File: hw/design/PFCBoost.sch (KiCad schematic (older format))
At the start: 34 parts

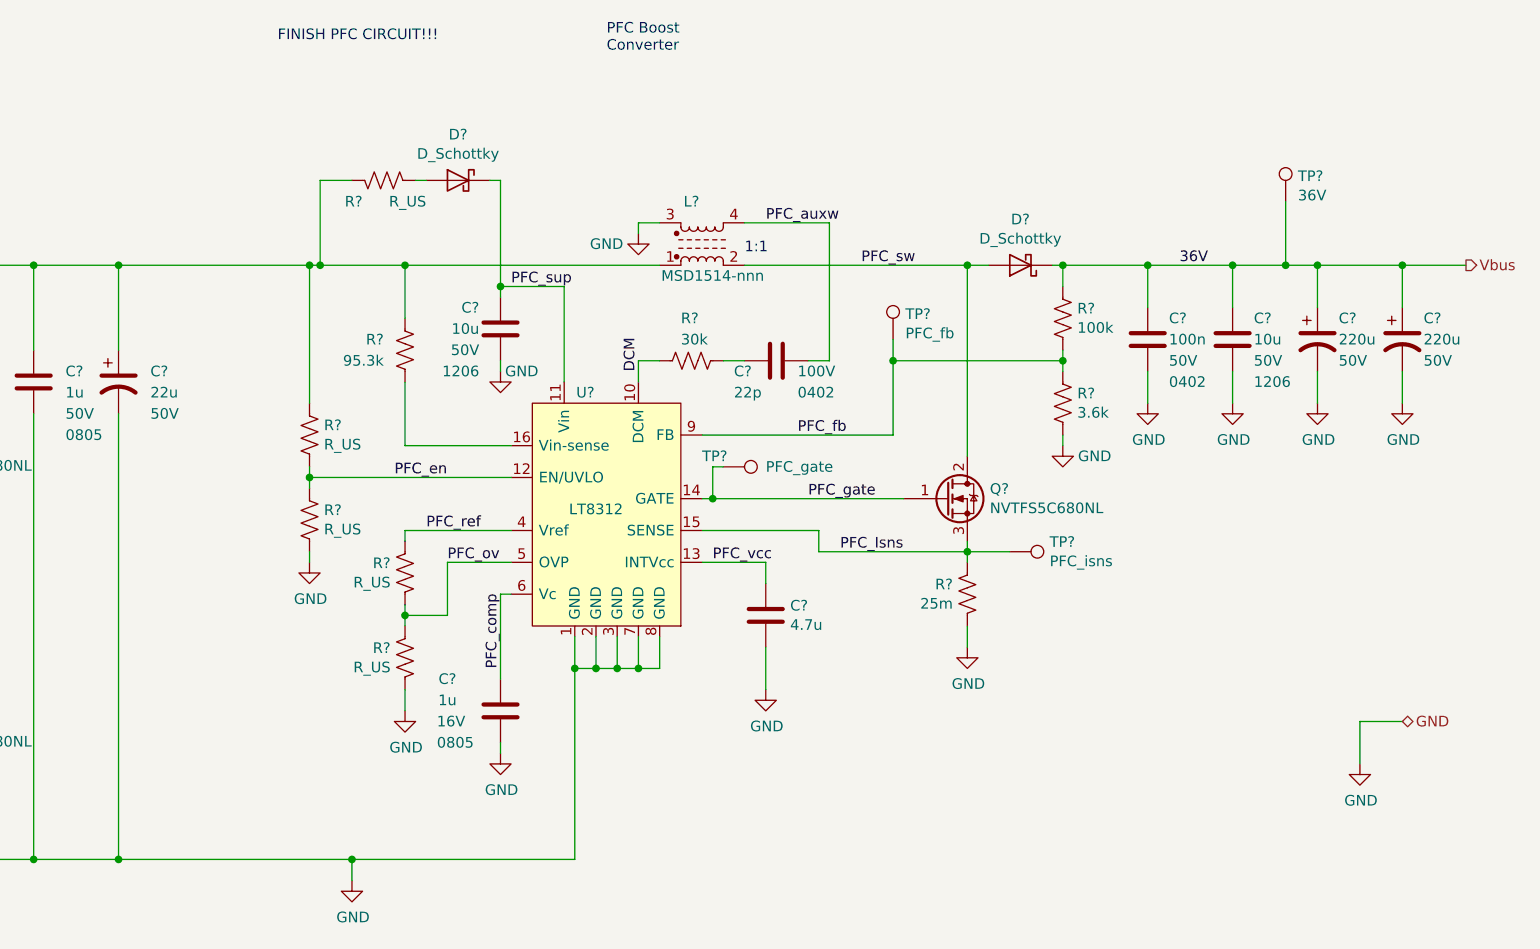
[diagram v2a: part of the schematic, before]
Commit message: lots of work
expanded README doc, specifications, added secondary regulator circuit + symbol, more component specs added
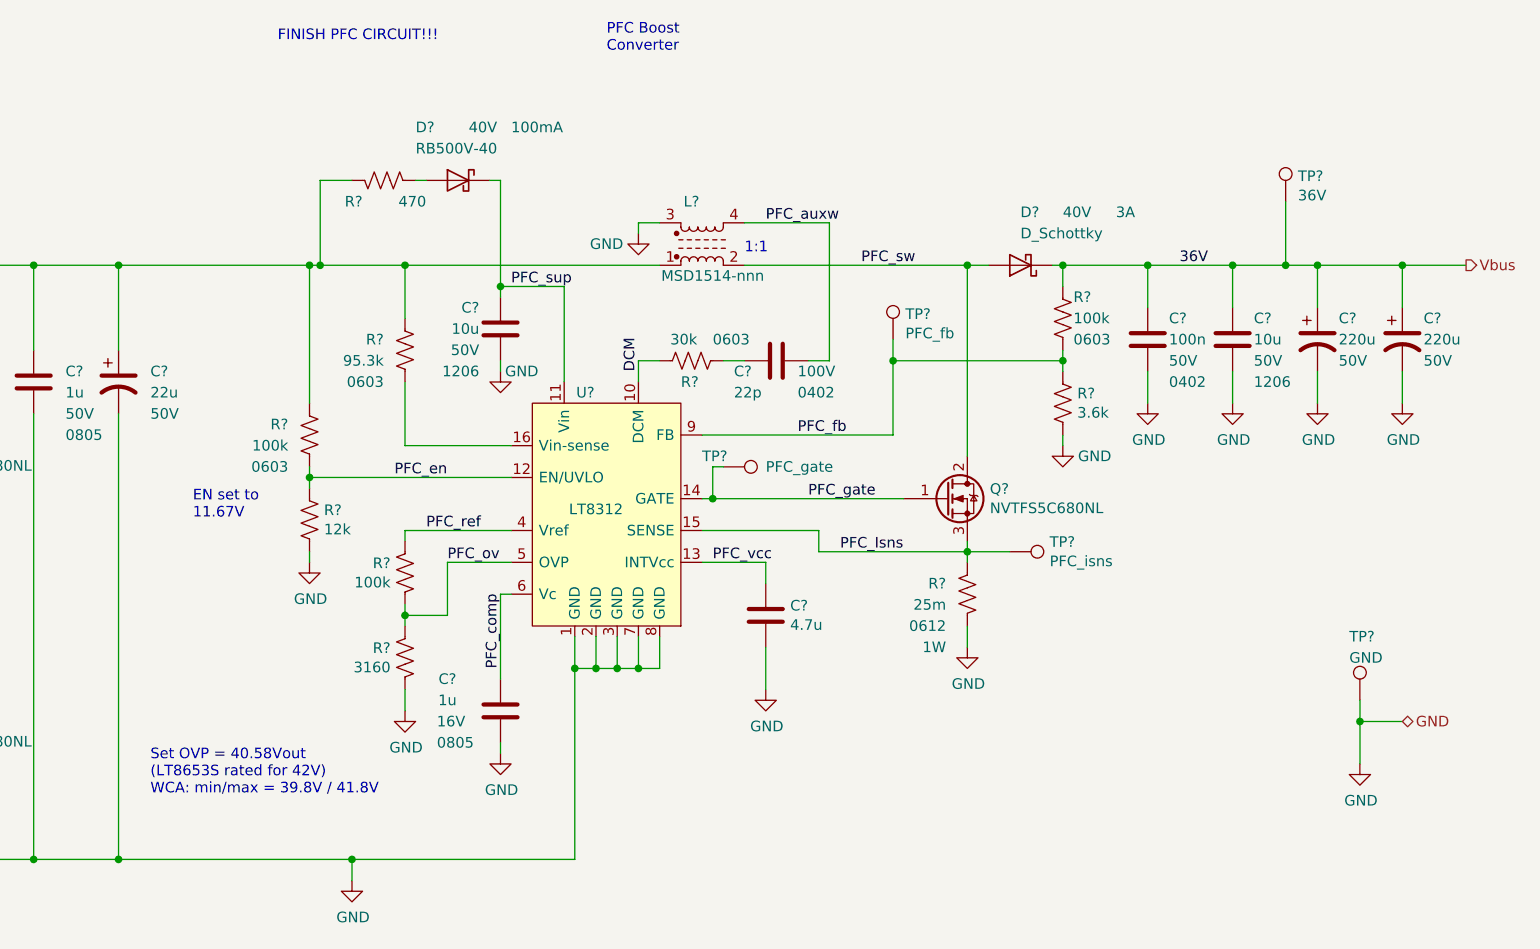
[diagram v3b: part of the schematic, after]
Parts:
- removed R?: R_US, Resistor_SMD:R_0603_1608Metric, symbol Device:R_US
- added R?: 100k, Resistor_SMD:R_0805_2012Metric_Pad1.15x1.40mm_HandSolder, symbol Device:R_US
- added TP?: GND, TestPoint:TestPoint_Keystone_5000-5004_Miniature, symbol Connector:TestPoint
- D?: value D_Schottky -> RB500V-40; MfrNum (none) -> TSMC_RB500V-40
- R?: value R_US -> 3160
- R?: value R_US -> 100k
- R?: PRating (none) -> 1W; Size (none) -> 0612
- R?: footprint Resistor_SMD:R_0805_2012Metric_Pad1.15x1.40mm_HandSolder -> Resistor_SMD:R_0805_2012Metric; Size (none) -> 0603
- R?: value R_US -> 12k
- R?: footprint Resistor_SMD:R_0603_1608Metric -> Resistor_SMD:R_0805_2012Metric; Size (none) -> 0603
- R?: value R_US -> 470; footprint Resistor_SMD:R_0603_1608Metric -> Resistor_SMD:R_0805_2012Metric
- R?: Size (none) -> 0603; VRating (none) -> 50
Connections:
- net GND: now also TP?.1
- net PFC_en: now also R?.2
- net P_rect: now also R?.1
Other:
- note added: "EN set to\n11.67V"
- note added: "Set OVP = 40.58Vout\n(LT8653S rated for 42V)\nWCA: min/max = 39.8V / 41.8V"
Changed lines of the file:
@@
 P 5900 3800
 F 0 "R?" H 5832 3754 50  0000 R CNN
-F 1 "R_US" H 5832 3845 50  0000 R CNN
+F 1 "3160" H 5832 3845 50  0000 R CNN
 F 2 "Resistor_SMD:R_0603_1608Metric" V 5940 3790 50  0001 C CNN
 F 3 "~" H 5900 3800 50  0001 C CNN
@@
 P 5900 3400
 F 0 "R?" H 5832 3354 50  0000 R CNN
-F 1 "R_US" H 5832 3445 50  0000 R CNN
+F 1 "100k" H 5832 3445 50  0000 R CNN
 F 2 "Resistor_SMD:R_0603_1608Metric" V 5940 3390 50  0001 C CNN
 F 3 "~" H 5900 3400 50  0001 C CNN
@@
 Connection ~ 4150 4750
 Wire Wire Line
-	4150 4750 4550 4750
-Wire Wire Line
 	4550 2650 4550 4750
-Connection ~ 4550 4750
 Wire Wire Line
 	6350 4200 6350 4250
@@
 U 1 1 5E8396C6
 P 8550 3500
-F 0 "R?" H 8482 3454 50  0000 R CNN
-F 1 "25m" H 8482 3545 50  0000 R CNN
+F 0 "R?" H 8450 3450 50  0000 R CNN
+F 1 "25m" H 8450 3550 50  0000 R CNN
 F 2 "Resistor_SMD:R_0612_1632Metric" V 8590 3490 50  0001 C CNN
 F 3 "~" H 8550 3500 50  0001 C CNN
+F 4 "0612" H 8450 3650 50  0000 R CNN "Size"
+F 5 "1W" H 8450 3750 50  0000 R CNN "PRating"
 	1    8550 3500
 	1    0    0    1
@@
 U 1 1 5EB6C5FB
 P 9000 2200
-F 0 "R?" H 8932 2154 50  0000 R CNN
-F 1 "100k" H 8932 2245 50  0000 R CNN
-F 2 "Resistor_SMD:R_0805_2012Metric_Pad1.15x1.40mm_HandSolder" V 9040 2190 50  0001 C CNN
+F 0 "R?" H 8950 2100 50  0000 R CNN
+F 1 "100k" H 8950 2200 50  0000 R CNN
+F 2 "Resistor_SMD:R_0805_2012Metric" V 9040 2190 50  0001 C CNN
 F 3 "~" H 9000 2200 50  0001 C CNN
+F 4 "0603" H 8950 2300 50  0000 R CNN "Size"
 	1    9000 2200
 	-1   0    0    1
@@
 $Comp
 L Device:R_US R?
-U 1 1 5EB79CFA
-P 5450 2750
-F 0 "R?" H 5382 2704 50  0000 R CNN
-F 1 "R_US" H 5382 2795 50  0000 R CNN
-F 2 "Resistor_SMD:R_0603_1608Metric" V 5490 2740 50  0001 C CNN
-F 3 "~" H 5450 2750 50  0001 C CNN
-	1    5450 2750
-	-1   0    0    1
-$EndComp
-$Comp
-L Device:R_US R?
 U 1 1 5EB79D44
 P 5450 3150
 F 0 "R?" H 5382 3104 50  0000 R CNN
-F 1 "R_US" H 5382 3195 50  0000 R CNN
+F 1 "12k" H 5382 3195 50  0000 R CNN
 F 2 "Resistor_SMD:R_0603_1608Metric" V 5490 3140 50  0001 C CNN
 F 3 "~" H 5450 3150 50  0001 C CNN
@@
 $EndComp
 $Comp
-L Device:R_US R?
-U 1 1 5EBD6503
-P 7250 2400
-F 0 "R?" V 7450 2450 50  0000 R CNN
-F 1 "30k" V 7350 2450 50  0000 R CNN
-F 2 "Resistor_SMD:R_0603_1608Metric" V 7290 2390 50  0001 C CNN
-F 3 "~" H 7250 2400 50  0001 C CNN
-	1    7250 2400
-	0    -1   -1   0
-$EndComp
-$Comp
 L power:GND #PWR?
 U 1 1 5EC0311F
@@
 Wire Wire Line
 	4550 1950 5450 1950
-Wire Wire Line
-	4550 4750 5650 4750
 $Comp
 L Device:R_US R?
@@
 P 5800 1550
 F 0 "R?" V 5700 1450 50  0000 R CNN
-F 1 "R_US" V 5700 1750 50  0000 R CNN
-F 2 "Resistor_SMD:R_0603_1608Metric" V 5840 1540 50  0001 C CNN
+F 1 "470" V 5700 1750 50  0000 R CNN
+F 2 "Resistor_SMD:R_0805_2012Metric" V 5840 1540 50  0001 C CNN
 F 3 "~" H 5800 1550 50  0001 C CNN
 	1    5800 1550
@@
 U 1 1 5EBAA43A
 P 8800 1950
-F 0 "D?" H 8800 1734 50  0000 C CNN
-F 1 "D_Schottky" H 8800 1825 50  0000 C CNN
+F 0 "D?" H 8800 1700 50  0000 R CNN
+F 1 "D_Schottky" H 8800 1800 50  0000 R CNN
 F 2 "Diode_SMD:D_SMB" H 8800 1950 50  0001 C CNN
 F 3 "~" H 8800 1950 50  0001 C CNN
-F 4 "40V" H 8800 1950 50  0001 C CNN "VRating"
-F 5 "3A" H 8800 1950 50  0001 C CNN "IRating"
+F 4 "40V" H 8600 1700 50  0000 R CNN "VRating"
+F 5 "3A" H 8350 1700 50  0000 R CNN "IRating"
 	1    8800 1950
 	-1   0    0    1
@@
 U 1 1 5EBF8B82
 P 6150 1550
-F 0 "D?" H 6150 1766 50  0000 C CNN
-F 1 "D_Schottky" H 6150 1675 50  0000 C CNN
+F 0 "D?" H 6350 1800 50  0000 R CNN
+F 1 "RB500V-40" H 6350 1700 50  0000 R CNN
 F 2 "Diode_SMD:D_SOD-123" H 6150 1550 50  0001 C CNN
 F 3 "~" H 6150 1550 50  0001 C CNN
-F 4 "40V" H 6150 1550 50  0001 C CNN "VRating"
-F 5 "100mA" H 6150 1550 50  0001 C CNN "IRating"
+F 4 "40V" H 6100 1800 50  0000 R CNN "VRating"
+F 5 "100mA" H 5900 1800 50  0000 R CNN "IRating"
+F 6 "TSMC_RB500V-40" H 6150 1550 50  0001 C CNN "MfrNum"
 	1    6150 1550
 	-1   0    0    -1
@@
 F 2 "Resistor_SMD:R_0805_2012Metric_Pad1.15x1.40mm_HandSolder" V 5940 2340 50  0001 C CNN
 F 3 "~" H 5900 2350 50  0001 C CNN
+F 4 "50" H 5900 2350 50  0001 C CNN "VRating"
+F 5 "0603" H 5800 2200 50  0000 R CNN "Size"
 	1    5900 2350
 	1    0    0    -1
@@
 Wire Wire Line
 	7500 1750 7900 1750
+$Comp
+L Device:R_US R?
+U 1 1 5EC990DA
+P 5450 2750
+F 0 "R?" H 5350 2800 50  0000 R CNN
+F 1 "100k" H 5350 2700 50  0000 R CNN
+F 2 "Resistor_SMD:R_0805_2012Metric_Pad1.15x1.40mm_HandSolder" V 5490 2740 50  0001 C CNN
+F 3 "~" H 5450 2750 50  0001 C CNN
+F 4 "50" H 5450 2750 50  0001 C CNN "VRating"
+F 5 "0603" H 5350 2600 50  0000 R CNN "Size"
+	1    5450 2750
+	1    0    0    -1
+$EndComp
+Connection ~ 4550 4750
+Wire Wire Line
+	4550 4750 5650 4750
+Wire Wire Line
+	4150 4750 4550 4750
+$Comp
+L Device:R_US R?
+U 1 1 5EBD6503
+P 7250 2400
+F 0 "R?" V 7150 2450 50  0000 R CNN
+F 1 "30k" V 7350 2500 50  0000 R CNN
+F 2 "Resistor_SMD:R_0805_2012Metric" V 7290 2390 50  0001 C CNN
+F 3 "~" H 7250 2400 50  0001 C CNN
+F 4 "0603" V 7350 2300 50  0000 R CNN "Size"
+	1    7250 2400
+	0    -1   -1   0
+$EndComp
+$Comp
+L Connector:TestPoint TP?
+U 1 1 5ECC8F09
+P 10400 4000
+AR Path="/5E80D1C0/5ECC8F09" Ref="TP?"  Part="1"
+AR Path="/5E80D210/5ECC8F09" Ref="TP?"  Part="1"
+AR Path="/5E84FADE/5ECC8F09" Ref="TP?"  Part="1"
+AR Path="/5ECFB146/5ECC8F09" Ref="TP?"  Part="1"
+F 0 "TP?" H 10350 4300 50  0000 L CNN
+F 1 "GND" H 10350 4200 50  0000 L CNN
+F 2 "TestPoint:TestPoint_Keystone_5000-5004_Miniature" H 10600 4000 50  0001 C CNN
+F 3 "~" H 10600 4000 50  0001 C CNN
+	1    10400 4000
+	1    0    0    -1
+$EndComp
+Wire Wire Line
+	10400 4000 10400 4100
+Connection ~ 10400 4100
+Text Notes 4700 4450 0    50   ~ 0
+Set OVP = 40.58Vout\n(LT8653S rated for 42V)\nWCA: min/max = 39.8V / 41.8V
+Text Notes 4900 3150 0    50   ~ 0
+EN set to\n11.67V
 $EndSCHEMATC

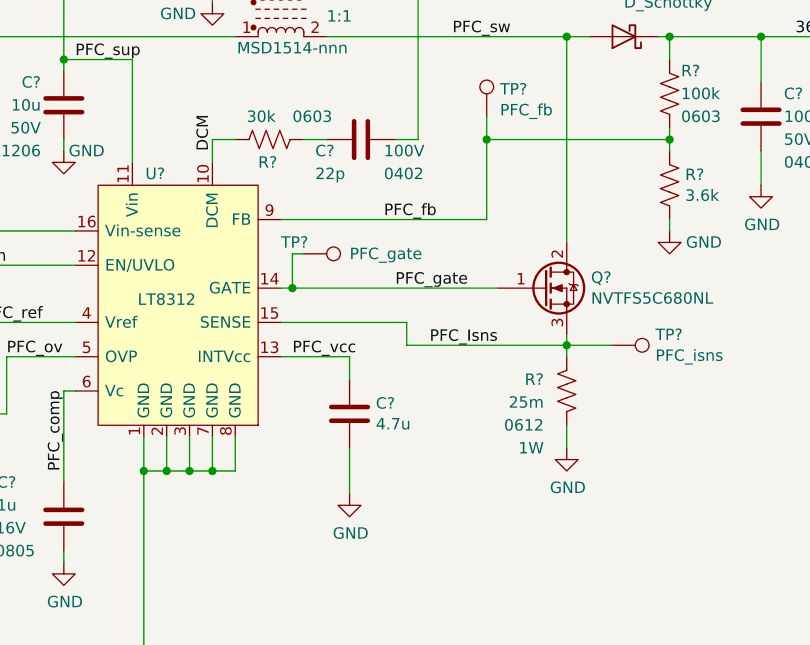
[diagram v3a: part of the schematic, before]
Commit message: updated PFC components
adjusted resistor sized, specified INTvcc capacitor
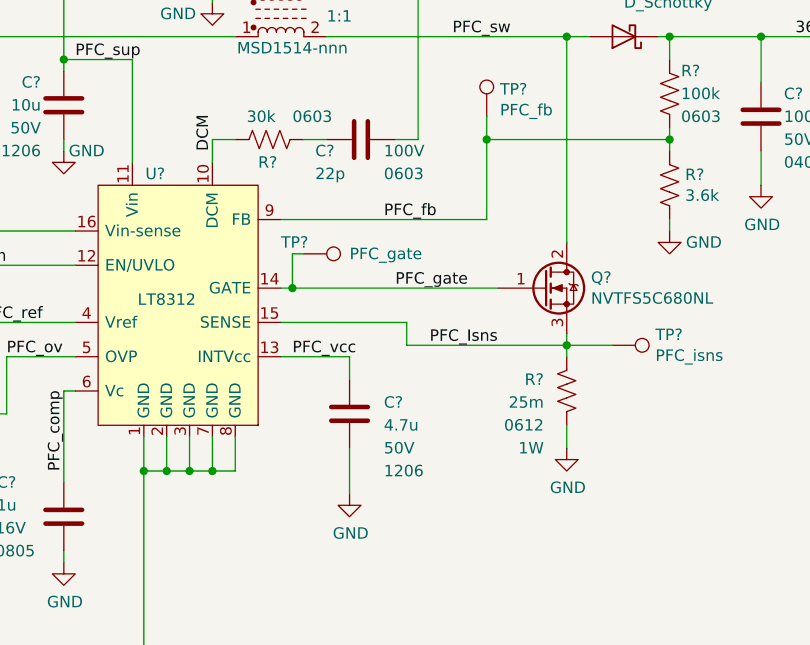
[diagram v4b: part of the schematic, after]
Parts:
- C?: footprint Capacitor_SMD:C_0805_2012Metric_Pad1.15x1.40mm_HandSolder -> Capacitor_SMD:C_1206_3216Metric_Pad1.42x1.75mm_HandSolder; MfrNum (none) -> Kemet_C1206C475K5RACTU; Size (none) -> 1206; VRating (none) -> 50V
- C?: Size 0402 -> 0603
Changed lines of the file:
@@
 U 1 1 5E81BE4D
 P 7600 3600
-F 0 "C?" H 7715 3646 50  0000 L CNN
-F 1 "4.7u" H 7715 3555 50  0000 L CNN
-F 2 "Capacitor_SMD:C_0805_2012Metric_Pad1.15x1.40mm_HandSolder" H 7638 3450 50  0001 C CNN
+F 0 "C?" H 7750 3650 50  0000 L CNN
+F 1 "4.7u" H 7750 3550 50  0000 L CNN
+F 2 "Capacitor_SMD:C_1206_3216Metric_Pad1.42x1.75mm_HandSolder" H 7638 3450 50  0001 C CNN
 F 3 "~" H 7600 3600 50  0001 C CNN
+F 4 "Kemet_C1206C475K5RACTU" H 7600 3600 50  0001 C CNN "MfrNum"
+F 5 "50V" H 7750 3450 50  0000 L CNN "VRating"
+F 6 "1206" H 7750 3350 50  0000 L CNN "Size"
 	1    7600 3600
 	1    0    0    -1
@@
 F 4 "findapart" V 7650 2400 50  0001 C CNN "MfrNum"
 F 5 "100V" V 7700 2500 50  0000 L CNN "VRating"
-F 6 "0402" V 7800 2500 50  0000 L CNN "Size"
+F 6 "0603" V 7800 2500 50  0000 L CNN "Size"
 	1    7650 2400
 	0    1    1    0

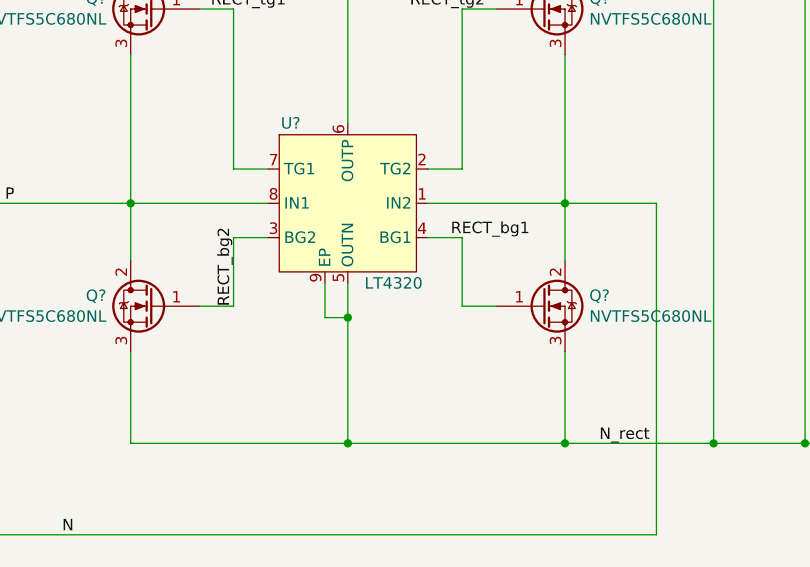
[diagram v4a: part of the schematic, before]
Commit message: more part numbers
Added manfacturer part numbers to ICs, added descriptions to symbols in library
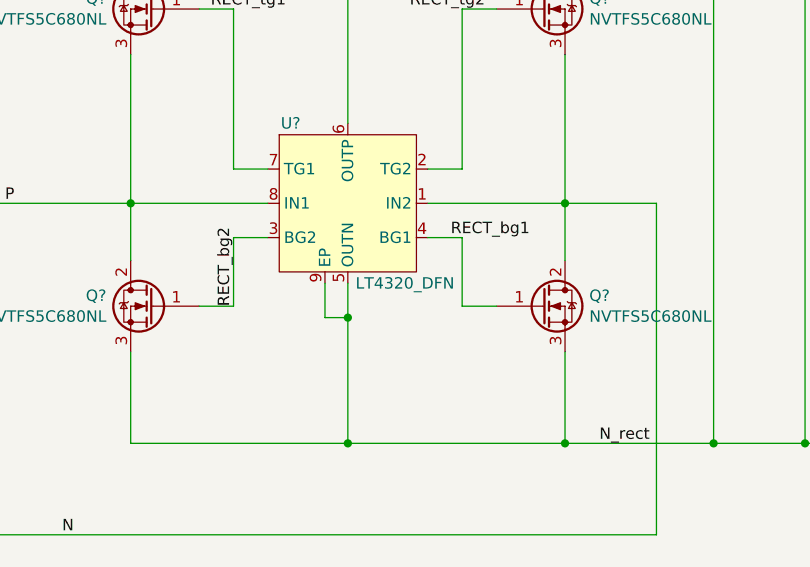
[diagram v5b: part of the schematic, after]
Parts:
- removed U?: LT4320, symbol pps_klib:LT4320
- added U?: LT4320_DFN, symbol pps_klib:LT4320_DFN
- U?: MfrNum (none) -> ADI_LT8312EMS
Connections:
- net GND: now also U?.5 (OUTN), U?.9 (EP)
- net N: now also U?.1 (IN2)
- net P: now also U?.8 (IN1)
- net P_rect: now also U?.6 (OUTP)
- net RECT_bg1: now also U?.4 (BG1)
- net RECT_bg2: now also U?.3 (BG2)
- net RECT_tg1: now also U?.7 (TG1)
- net RECT_tg2: now also U?.2 (TG2)
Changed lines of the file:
@@
 F 2 "" H 7000 3500 50  0001 C CNN
 F 3 "" H 7000 3500 50  0001 C CNN
+F 4 "ADI_LT8312EMS" H 6850 3100 50  0001 C CNN "MfrNum"
 	1    6850 3100
-	1    0    0    -1
-$EndComp
-$Comp
-L pps_klib:LT4320 U?
-U 1 1 5EC55A62
-P 2550 3700
-F 0 "U?" H 2300 4050 50  0000 C CNN
-F 1 "LT4320" H 2750 3350 50  0000 C CNN
-F 2 "" H 2550 3700 50  0001 C CNN
-F 3 "" H 2550 3700 50  0001 C CNN
-	1    2550 3700
 	1    0    0    -1
 $EndComp
@@
 Text Notes 4900 3150 0    50   ~ 0
 EN set to\n11.67V
+$Comp
+L pps_klib:LT4320_DFN U?
+U 1 1 5ECBE116
+P 2550 3700
+F 0 "U?" H 2300 4050 50  0000 C CNN
+F 1 "LT4320_DFN" H 2800 3350 50  0000 C CNN
+F 2 "" H 2550 3700 50  0001 C CNN
+F 3 "" H 2550 3700 50  0001 C CNN
+F 4 "ADI_LT4320IDD" H 2550 3700 50  0001 C CNN "MfrNum"
+	1    2550 3700
+	1    0    0    -1
+$EndComp
 $EndSCHEMATC
